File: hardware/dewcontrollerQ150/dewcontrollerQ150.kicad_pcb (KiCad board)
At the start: 2 copper layers, 54.1 x 52 mm, 17 parts, among them J1 12V Power, J2 Dew Heater, J3 SHT45 Sensor, Q1 FQP 30N06L, U2 Buck_12V_5V, U3 XIAO-ESP32-S3-DIP

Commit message: v0.7 Latest CAD and KiCAD files
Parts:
- moved R2 36.0 mm to (184.1, 93.3), turned to -90 degrees
- moved Q1 32.0 mm to (173.2, 87.1), turned to 0 degrees
- moved C1 30.0 mm to (182.5, 110.2), turned to 0 degrees
- moved C2 25.2 mm to (161.2, 87.4)
- moved C3 24.7 mm to (144.2, 101.2)
- moved R1 24.7 mm to (173.1, 92.2)
- moved C4 24.3 mm to (152.5, 101.1)
- moved R3 21.5 mm to (160.1, 100.3), turned to -90 degrees
- moved J3 19.4 mm to (133.3, 110.2), turned to 90 degrees
- moved mh3 6.60 mm to (187.1, 119.2)
- moved mh2 6.17 mm to (187.1, 77.7)
- moved U2 2.98 mm to (170.7, 106.3)
- moved mh4 2.24 mm to (133.3, 119.2)
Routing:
- net +12V: track 0.00 -> 68.0 mm
- net /5V: track 31.0 -> 83.6 mm, vias 0 -> 1
- net 12V Return: track 0.00 -> 46.7 mm
- net Net-(U3-GPIO7/D8/A8/SCK): track 0.00 -> 17.8 mm
- net Net-(Q1-G): track 0.00 -> 13.5 mm
- net Net-(U2-EN): track 0.00 -> 13.0 mm
- net /3.3V: track 46.4 -> 34.0 mm
- net /SCL: track 35.2 -> 23.7 mm
- net /-Heater: track 0.00 -> 11.4 mm
- net /SDA: track 39.0 -> 32.4 mm, vias 0 -> 1
- added copper zone on B.Cu, net GND
- added copper zone on F.Cu, net GND
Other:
- board size 54.1 x 52 mm -> 60.9 x 49.8 mm
- board text added: "+"
- board text added: "12V"
- board text added: "12V IN"
- board text added: "3.3V"
- board text added: "5V"
- board text added: "BUCK 12->5"
- board text added: "ESP32-S3"
- board text added: "Gnd"
- board text added: "Heater"
- board text added: "Q150DewController Rev A"
- board text added: "SCL"
- board text added: "SDA"
- board text added: "SHT45"
- board text added: "o"

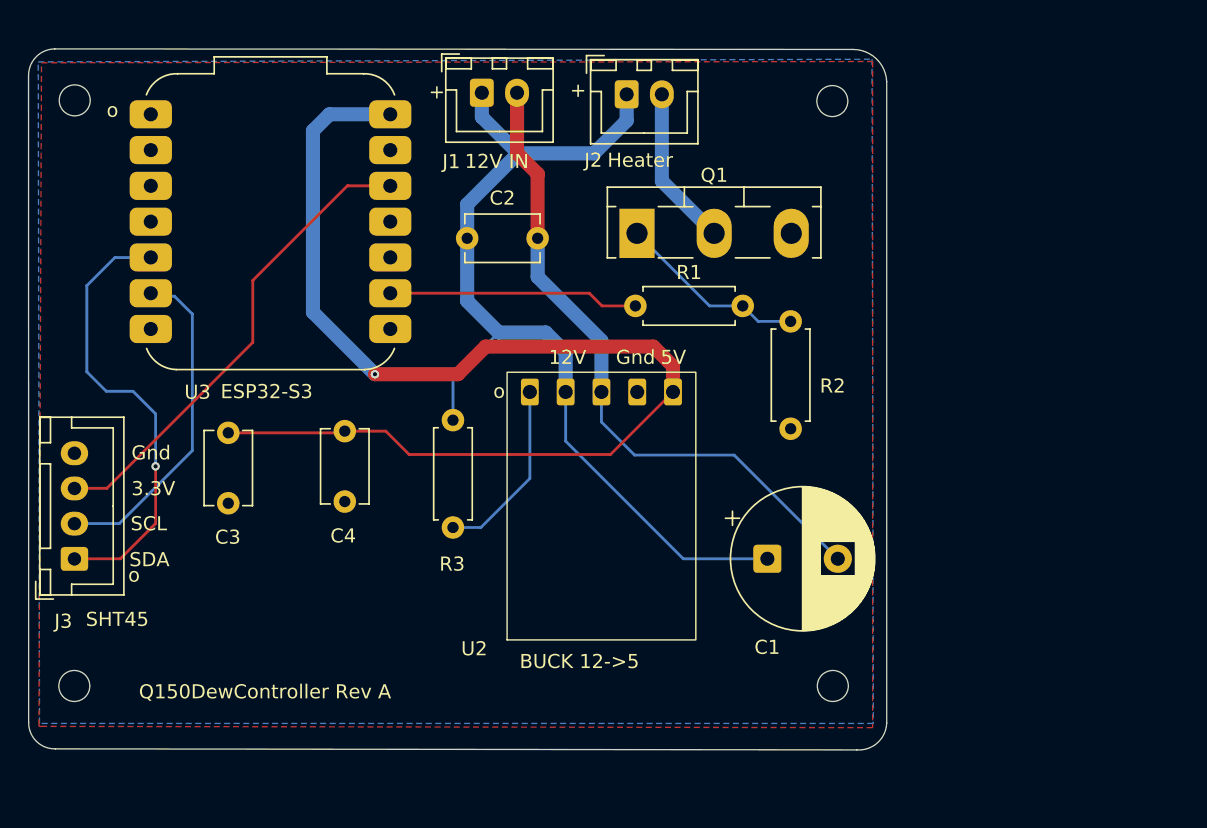
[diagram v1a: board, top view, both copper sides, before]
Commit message: V1.2 PCB fixed ESP32S3 and FQP30N06 footprints
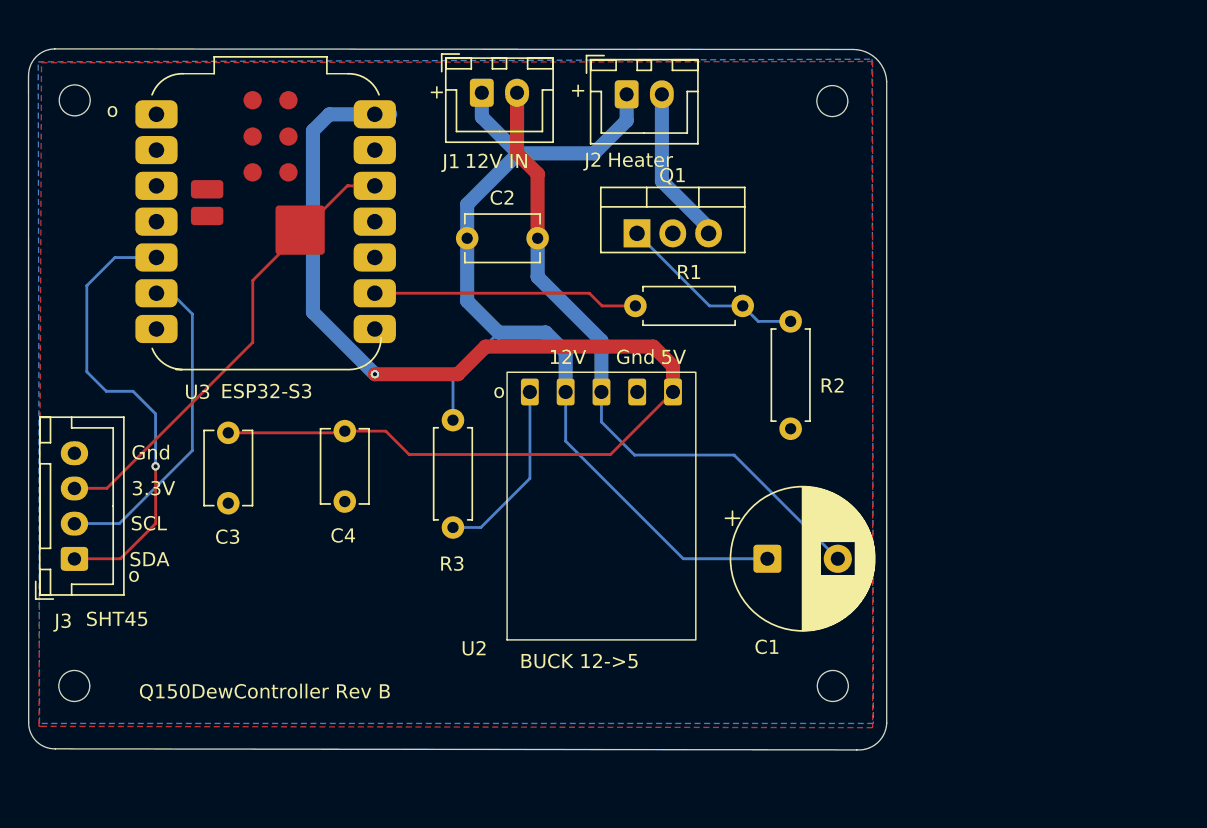
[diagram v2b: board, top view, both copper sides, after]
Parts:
- Q1: footprint Package_TO_SOT_THT:TO-218-3_Vertical -> Package_TO_SOT_THT:TO-220-3_Vertical
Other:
- board text added: "Q150DewController Rev B"
- board text removed: "Q150DewController Rev A"

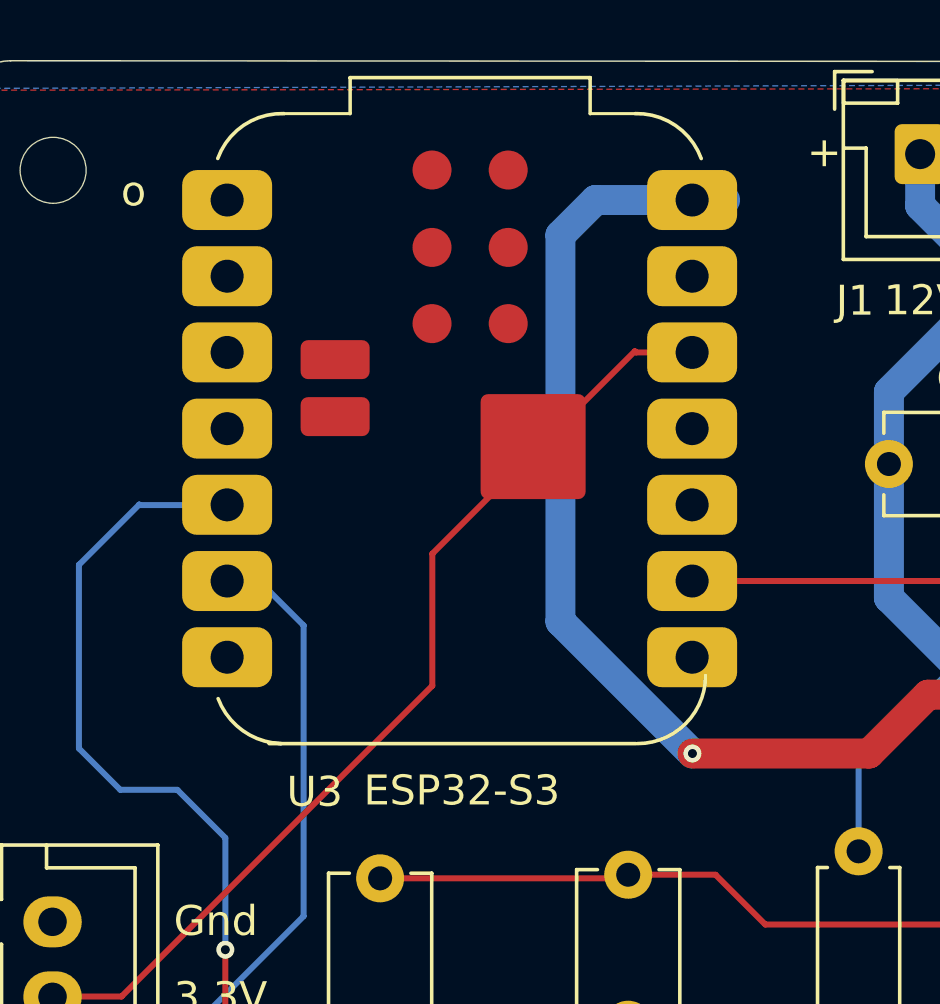
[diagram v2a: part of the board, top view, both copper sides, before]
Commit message: v1.2b Changed esp32-S3 to correct footprint
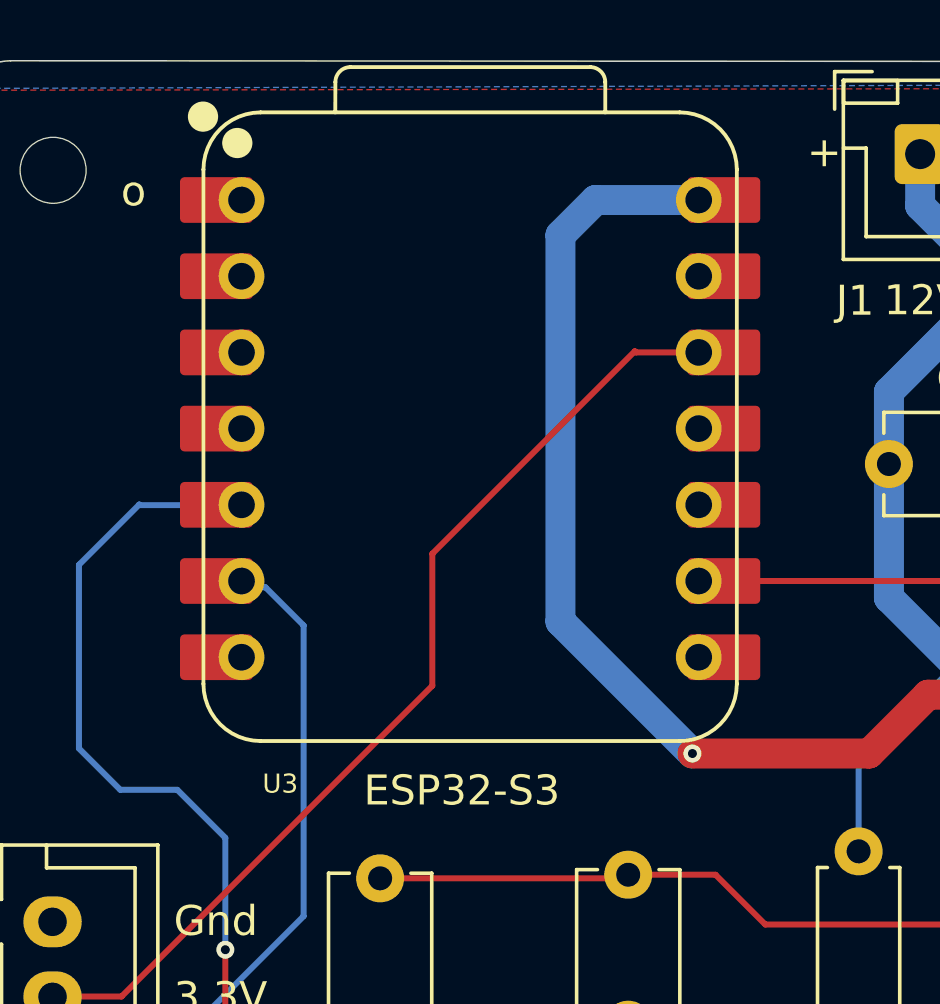
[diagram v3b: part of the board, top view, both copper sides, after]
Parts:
- U3: footprint RF_Module:MCU_Seeed_ESP32C3 -> Seeed Studio XIAO Series Library:XIAO-ESP32S3-DIP
